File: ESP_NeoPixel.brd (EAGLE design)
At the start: 25.6 x 34.1 mm, 15 parts, among them J3 MKDS3-2-5.00, J4 MKDS3-3-5.00, Q1 BSN20,215, U1 LMZ21700

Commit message: leds
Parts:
- added LED1, LED2: (no value), led:CHIP-LED0603
- added R5, R6: (no value), rcl:R0603
- J1, J2: value (none) -> CONN_08; device SparkFun-Connectors:1X08_LOCK_NO_SILK -> jonas_Sparkfun-Connectors:1X08_LOCK_NO_SILK
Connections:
- new net N$3: LED1.A, R5.1
- new net N$4: LED2.A, R6.1
- net D6: now also R5.2
- net D7: now also R6.2
- net GND: now also LED1.C, LED2.C
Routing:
- net D7: track 0.00 -> 3.35 mm
- net +3V3: track 13.3 -> 16.4 mm
- net GND: track 5.70 -> 8.75 mm, vias 24 -> 25
- net D6: track 0.00 -> 2.91 mm
- net N$4: track 0.00 -> 1.40 mm
- net N$3: track 0.00 -> 1.40 mm
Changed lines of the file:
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@@
 </layers>
 <board>
+<fusionsync huburn="a.cGVyc29uYWw6dWUyOTRlNWI0" projecturn="a.cGVyc29uYWw6dWUyOTRlNWI0IzIwMTgwOTMwMTUxNzM0NzMx" f3durn="urn:adsk.wipprod:dm.lineage:7b53gxeNQ0mJTjwWGVlYEQ" pcbguid="beee229b-ca1a-41e8-b53f-387b8cffb208" lastpulledtime="" lastsyncedchangeguid="99687992-9acd-0b6a-2775-a8b7a6ba92e0"/>
 <plain>
 <wire x1="12.8" y1="-8.65" x2="12.8" y2="21.5" width="0" layer="20"/>
@@
 </autorouter>
 <elements>
-<element name="J1" library="SparkFun-Connectors" library_urn="urn:adsk.eagle:library:513" package="1X08_LOCK_NO_SILK" package3d_urn="urn:adsk.eagle:package:38147/1" value="" x="-11.43" y="0" rot="R90">
+<element name="J1" library="jonas_Sparkfun-Connectors" library_urn="urn:adsk.eagle:library:3855661" package="1X08_LOCK_NO_SILK" package3d_urn="urn:adsk.eagle:package:3855663/2" value="CONN_08" x="-11.43" y="0" rot="R90">
 <attribute name="VALUE" x="-9.398" y="-1.27" size="0.6096" layer="27" font="vector" ratio="20" rot="R90"/>
 </element>
-<element name="J2" library="SparkFun-Connectors" library_urn="urn:adsk.eagle:library:513" package="1X08_LOCK_NO_SILK" package3d_urn="urn:adsk.eagle:package:38147/1" value="" x="11.43" y="0" rot="R90">
+<element name="J2" library="jonas_Sparkfun-Connectors" library_urn="urn:adsk.eagle:library:3855661" package="1X08_LOCK_NO_SILK" package3d_urn="urn:adsk.eagle:package:3855663/2" value="CONN_08" x="11.43" y="0" rot="R90">
 <attribute name="VALUE" x="13.462" y="-1.27" size="0.6096" layer="27" font="vector" ratio="20" rot="R90"/>
 </element>
@@
 <attribute name="MF" value="NXP Semiconductors" x="-7" y="10" size="1.778" layer="27" rot="R90" display="off"/>
 <attribute name="MP" value="BSN20,215" x="-7" y="10" size="1.778" layer="27" rot="R90" display="off"/>
-<attribute name="NAME" x="-7" y="8" size="0.8128" layer="25" font="vector" align="top-center"/>
+<attribute name="NAME" x="-9" y="11.7" size="0.8128" layer="25" font="vector" align="top-center"/>
 <attribute name="PACKAGE" value="TO-236 NXP Semiconductors" x="-7" y="10" size="1.778" layer="27" rot="R90" display="off"/>
 <attribute name="PRICE" value="0.17 USD" x="-7" y="10" size="1.778" layer="27" rot="R90" display="off"/>
 </element>
 <element name="R3" library="rcl" library_urn="urn:adsk.eagle:library:334" package="R0603" package3d_urn="urn:adsk.eagle:package:23555/2" value="4.7k" x="-4" y="10" rot="R270">
-<attribute name="NAME" x="-4" y="8" size="0.8128" layer="25" font="vector" align="top-center"/>
+<attribute name="NAME" x="-2.9" y="11" size="0.8128" layer="25" font="vector" rot="R180" align="center-right"/>
 <attribute name="SPICEPREFIX" value="R" x="1" y="10" size="1.778" layer="27" rot="R270" display="off"/>
 <attribute name="VALUE" x="-5.905" y="10.635" size="1.27" layer="27" rot="R270"/>
@@
 </element>
 <element name="LOGO1" library="SparkFun-Aesthetics" library_urn="urn:adsk.eagle:library:507" package="OSHW-LOGO-S" package3d_urn="urn:adsk.eagle:package:37099/1" value="OSHW-LOGOS" x="9.8" y="22.5"/>
+<element name="LED1" library="led" library_urn="urn:adsk.eagle:library:259" package="CHIP-LED0603" package3d_urn="urn:adsk.eagle:package:15819/3" value="" x="-4.8" y="7" rot="R270">
+<attribute name="NAME" x="-1" y="7" size="0.8128" layer="25" font="vector" align="center-right"/>
+<attribute name="VALUE" x="-5.435" y="5.095" size="1.27" layer="27"/>
+</element>
+<element name="R5" library="rcl" library_urn="urn:adsk.eagle:library:334" package="R0603" package3d_urn="urn:adsk.eagle:package:23555/2" value="" x="-7.8" y="7" rot="R180">
+<attribute name="NAME" x="-8" y="5.6" size="0.8128" layer="25" font="vector" align="center-right"/>
+<attribute name="SPICEPREFIX" value="R" x="-7.8" y="7" size="1.778" layer="27" rot="R180" display="off"/>
+<attribute name="VALUE" x="-7.165" y="8.905" size="1.27" layer="27" rot="R180"/>
+</element>
+<element name="LED2" library="led" library_urn="urn:adsk.eagle:library:259" package="CHIP-LED0603" package3d_urn="urn:adsk.eagle:package:15819/3" value="" x="-4.8" y="4" rot="R270">
+<attribute name="NAME" x="-1" y="4" size="0.8128" layer="25" font="vector" align="center-right"/>
+<attribute name="VALUE" x="5.565" y="7.095" size="1.27" layer="27"/>
+</element>
+<element name="R6" library="rcl" library_urn="urn:adsk.eagle:library:334" package="R0603" package3d_urn="urn:adsk.eagle:package:23555/2" value="" x="-7.8" y="4" rot="R180">
+<attribute name="NAME" x="-8" y="2.6" size="0.8128" layer="25" font="vector" align="center-right"/>
+<attribute name="SPICEPREFIX" value="R" x="-2.8" y="4" size="1.778" layer="27" rot="R180" display="off"/>
+<attribute name="VALUE" x="-2.165" y="5.905" size="1.27" layer="27" rot="R180"/>
+</element>
 </elements>
 <signals>
@@
 <signal name="D6">
 <contactref element="J1" pad="4"/>
+<contactref element="R5" pad="2"/>
+<wire x1="-11.303" y1="7.62" x2="-9.27" y2="7.62" width="0.1778" layer="1"/>
+<wire x1="-9.27" y1="7.62" x2="-8.65" y2="7" width="0.1778" layer="1"/>
 </signal>
 <signal name="D7">
 <contactref element="J1" pad="3"/>
+<contactref element="R6" pad="2"/>
+<wire x1="-11.557" y1="5.08" x2="-9.73" y2="5.08" width="0.1778" layer="1"/>
+<wire x1="-9.73" y1="5.08" x2="-8.65" y2="4" width="0.1778" layer="1"/>
 </signal>
 <signal name="D8">
@@
 <wire x1="11.557" y1="2.54" x2="9.84" y2="2.54" width="1.27" layer="16"/>
 <wire x1="9.84" y1="2.54" x2="9" y2="1.7" width="1.27" layer="16"/>
+<contactref element="LED1" pad="C"/>
+<contactref element="LED2" pad="C"/>
+<wire x1="-4.05" y1="4" x2="-4" y2="4.05" width="0.1778" layer="1"/>
+<wire x1="-4" y1="4.05" x2="-4" y2="5.5" width="0.1778" layer="1"/>
+<via x="-4" y="5.5" extent="1-16" drill="0.35"/>
+<wire x1="-4" y1="5.5" x2="-4" y2="6.95" width="0.1778" layer="1"/>
+<wire x1="-4" y1="6.95" x2="-4.05" y2="7" width="0.1778" layer="1"/>
 </signal>
 <signal name="+3V3">
@@
 <contactref element="Q1" pad="1"/>
 <contactref element="R3" pad="2"/>
-<wire x1="-11.557" y1="0" x2="-5.9" y2="5.657" width="0.1778" layer="1"/>
-<wire x1="-5.9" y1="5.657" x2="-5.9" y2="9.05" width="0.1778" layer="1"/>
 <wire x1="-5.9" y1="9.05" x2="-4.1" y2="9.05" width="0.1778" layer="1"/>
 <wire x1="-4.1" y1="9.05" x2="-4" y2="9.15" width="0.1778" layer="1"/>
+<wire x1="-11.557" y1="0" x2="-7.8" y2="0" width="0.1778" layer="1"/>
+<wire x1="-7.8" y1="0" x2="-4.8" y2="3" width="0.1778" layer="1"/>
+<wire x1="-4.8" y1="3" x2="-4.8" y2="7.5" width="0.1778" layer="1"/>
+<wire x1="-4" y1="8.3" x2="-4" y2="9.15" width="0.1778" layer="1"/>
+<wire x1="-4.8" y1="7.5" x2="-4" y2="8.3" width="0.1778" layer="1"/>
 </signal>
 <signal name="VCC">
@@
 <wire x1="2.79" y1="8.64" x2="2" y2="7.85" width="0.1778" layer="1"/>
 </signal>
+<signal name="N$3">
+<contactref element="LED1" pad="A"/>
+<contactref element="R5" pad="1"/>
+<wire x1="-6.95" y1="7" x2="-5.55" y2="7" width="0.1778" layer="1"/>
+</signal>
+<signal name="N$4">
+<contactref element="LED2" pad="A"/>
+<contactref element="R6" pad="1"/>
+<wire x1="-6.95" y1="4" x2="-5.55" y2="4" width="0.1778" layer="1"/>
+</signal>
 </signals>
 <mfgpreviewcolors>
@@
 </note>
 <note version="8.3" severity="warning">
+Since Version 8.3, EAGLE supports Fusion synchronisation.
+This feature will not be available in this version and saving
+the document will break the link to the Fusion PCB feature.
+</note>
+<note version="8.3" severity="warning">

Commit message: various layout changes
used sparkfun libraries
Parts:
- C1, C3: value 22µF -> 22uF; device rcl:C0805 -> SparkFun-Capacitors:0805
- C2: device rcl:C0603 -> SparkFun-Capacitors:0603
- LED1, LED2: device led:CHIP-LED0603 -> SparkFun-LED:LED-0603
- LOGO1: value OSHW-LOGOS -> OSHW-LOGO; device SparkFun-Aesthetics:OSHW-LOGO-S -> jonas_SparkFun-Aesthetics:OSHW-LOGO-M
- R1, R2, R3, R4: device rcl:R0603 -> SparkFun-Resistors:0603
- R5, R6: value (none) -> (none); device rcl:R0603 -> SparkFun-Resistors:0603
- moved LED1 2.53 mm to (-7.20, 6.20), turned to 180 degrees
- moved LED2 2.47 mm to (-7.20, 3.40), turned to 180 degrees
- moved R4 1.51 mm to (-6.50, 12.8)
- moved R6 1.00 mm to (-7.20, 4.80)
- moved R5 0.85 mm to (-7.20, 7.60)
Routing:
- net +5V: track 37.4 -> 42.2 mm
- net VCC: track 42.4 -> 46.6 mm
- net GND: track 8.75 -> 7.16 mm, vias 25 -> 26
- net NEOPIX_5V: track 14.0 -> 15.4 mm
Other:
- board text added: "- +"
- board text added: "-S+"
- board text removed: "+S-"

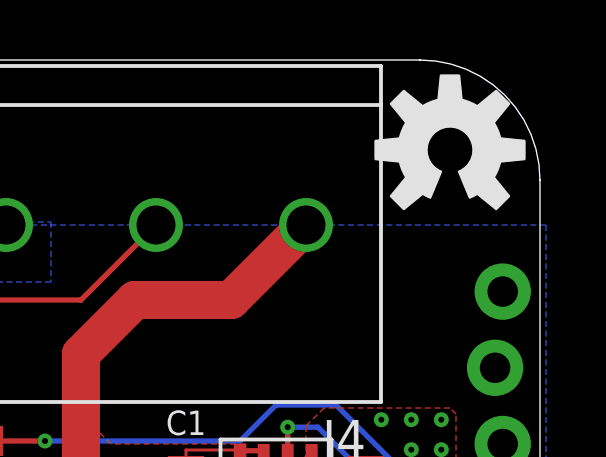
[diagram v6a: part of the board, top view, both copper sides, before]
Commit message: silkscreen fixes
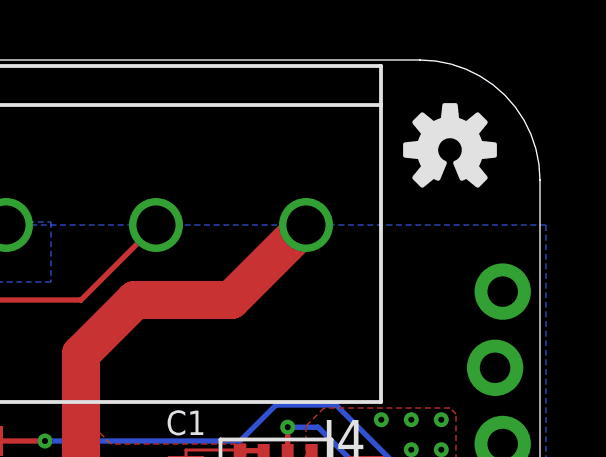
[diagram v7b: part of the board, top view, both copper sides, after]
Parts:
- LOGO1: value OSHW-LOGO -> OSHW-LOGOS; device jonas_SparkFun-Aesthetics:OSHW-LOGO-M -> SparkFun-Aesthetics:OSHW-LOGO-S
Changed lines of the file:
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@@
 <text x="-8" y="21" size="1.778" layer="21" rot="R180" align="center-left">-S+</text>
 <text x="0" y="17" size="2.54" layer="22" rot="MR0" align="center">+ S -</text>
-<text x="2" y="11" size="1.778" layer="22" ratio="12" rot="MR90" align="bottom-right">github.com
+<text x="-8" y="11" size="1.778" layer="22" ratio="12" rot="MR90" align="bottom-right">github.com
 /ottojo
 /wifiblink</text>
@@
 <attribute name="VALUE" value="1nF" x="0.095" y="7.635" size="1.27" layer="27" rot="R270"/>
 </element>
-<element name="LOGO1" library="jonas_SparkFun-Aesthetics" library_urn="urn:adsk.eagle:library:3855705" package="OSHW-LOGO-M" package3d_urn="urn:adsk.eagle:package:3855707/2" value="OSHW-LOGO" x="9.8" y="22.5"/>
+<element name="LOGO1" library="SparkFun-Aesthetics" library_urn="urn:adsk.eagle:library:507" package="OSHW-LOGO-S" package3d_urn="urn:adsk.eagle:package:37099/1" value="OSHW-LOGOS" x="9.8" y="22.5"/>
 <element name="LED1" library="SparkFun-LED" library_urn="urn:adsk.eagle:library:529" package="LED-0603" package3d_urn="urn:adsk.eagle:package:39354/1" value="" x="-7.2" y="6.2" rot="R180">
 <attribute name="NAME" x="-5.2" y="6.2" size="0.8128" layer="25" font="vector" rot="R180" align="center-right"/>
